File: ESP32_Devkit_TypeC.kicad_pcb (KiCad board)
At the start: 2 copper layers, 25.3 x 48.2 mm, 48 parts, among them J1 USB_C_Receptacle_USB2.0, J2 Conn_01x19, J3 Conn_01x19, Q1 SS8050, Q2 SS8050, SW1 EN, SW2 BOOT, U1 MP2359, U2 CH340G, U3 ESP32-PICO-D4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

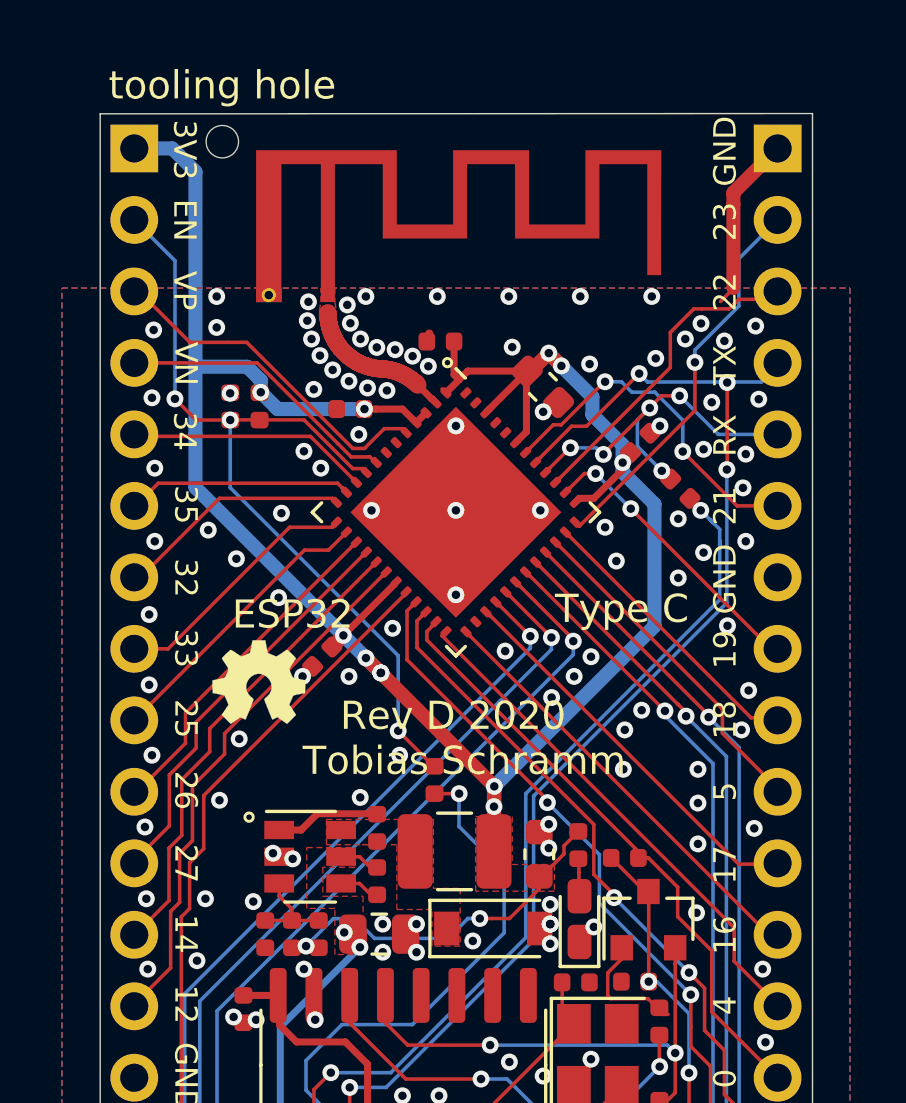
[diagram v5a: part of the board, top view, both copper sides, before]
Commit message: Rev E better bypassing
This revision improves upon the bypassing of the ESP32 Pico D4.
The previous bypassing was not satisfactory to me and I fear it
might cause issues under high load conditions.
Bypassing is improved by adding an additional 10uF capacitor to
each power pin.
Additionally a third 22uF capacitor has been added to icrease bulk
capacitance
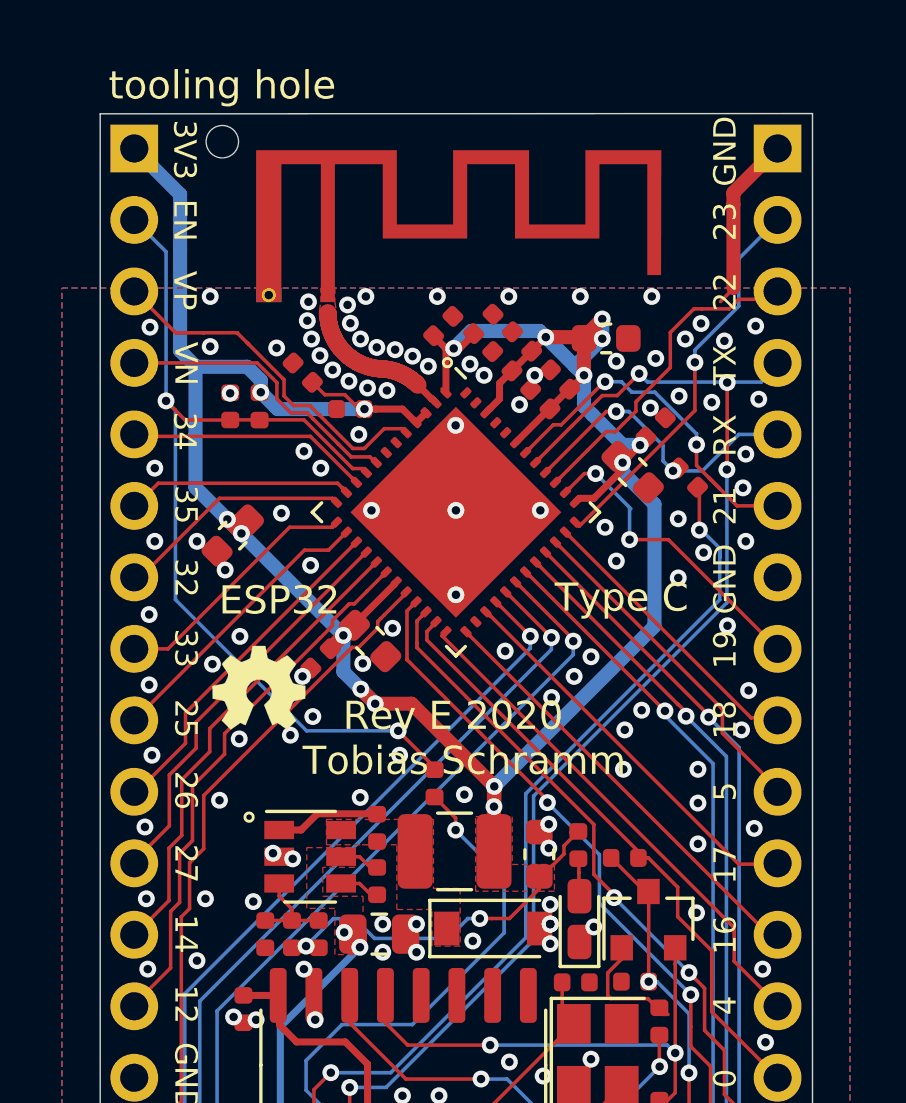
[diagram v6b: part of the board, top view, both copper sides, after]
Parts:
- added C17: 100 nF, Capacitor_SMD:C_0402_1005Metric, F.Cu at (101.7, 84.7)
- added C18: 100 nF, Capacitor_SMD:C_0402_1005Metric, F.Cu at (103.0, 86.0)
- added C19: 10uF, Capacitor_SMD:C_0402_1005Metric, F.Cu at (102.3, 84.0)
- added C20: 10uF, Capacitor_SMD:C_0402_1005Metric, F.Cu at (101.0, 83.4)
- added C21: 10uF, Capacitor_SMD:C_0402_1005Metric, F.Cu at (103.7, 85.3)
- added C22: 10uF, Capacitor_SMD:C_0402_1005Metric, F.Cu at (94.6, 85.1)
- added C23: 10uF, Capacitor_SMD:C_0603_1608Metric, F.Cu at (97.0, 94.6)
- added C24: 22 uF, Capacitor_SMD:C_0603_1608Metric, F.Cu at (92.1, 90.9)
- added C25: 10uF, Capacitor_SMD:C_0603_1608Metric, F.Cu at (106.3, 88.6)
- moved C13 2.83 mm to (105.3, 83.9), turned to 0 degrees
- moved C6 0.77 mm to (107.1, 87.1)
- moved C15 0.56 mm to (99.5, 83.5), turned to 225 degrees
- moved R4 0.48 mm to (108.2, 88.8)
- moved I2 0.20 mm to (93.0, 96.3)
- moved R11 0.12 mm to (99.2, 99.7)
- moved C16 0.08 mm to (95.2, 95.3)
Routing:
- net +3V3: track 95.0 -> 109.5 mm, vias 13 -> 18
- net /EN: track 30.2 -> 34.0 mm, vias 3 -> 2
- net /RXD: track 13.3 -> 11.1 mm, vias 5 -> 2
- net /IO19: track 10.5 -> 11.3 mm
- net Net-(C10-Pad2): track 48.7 -> 48.1 mm
- net /IO21: track 12.7 -> 13.2 mm
- net /VP: track 12.2 -> 12.8 mm
- net GND: track 6.74 -> 6.70 mm, vias 139 -> 145
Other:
- board text added: "Rev E 2020"
- board text removed: "Rev D 2020"

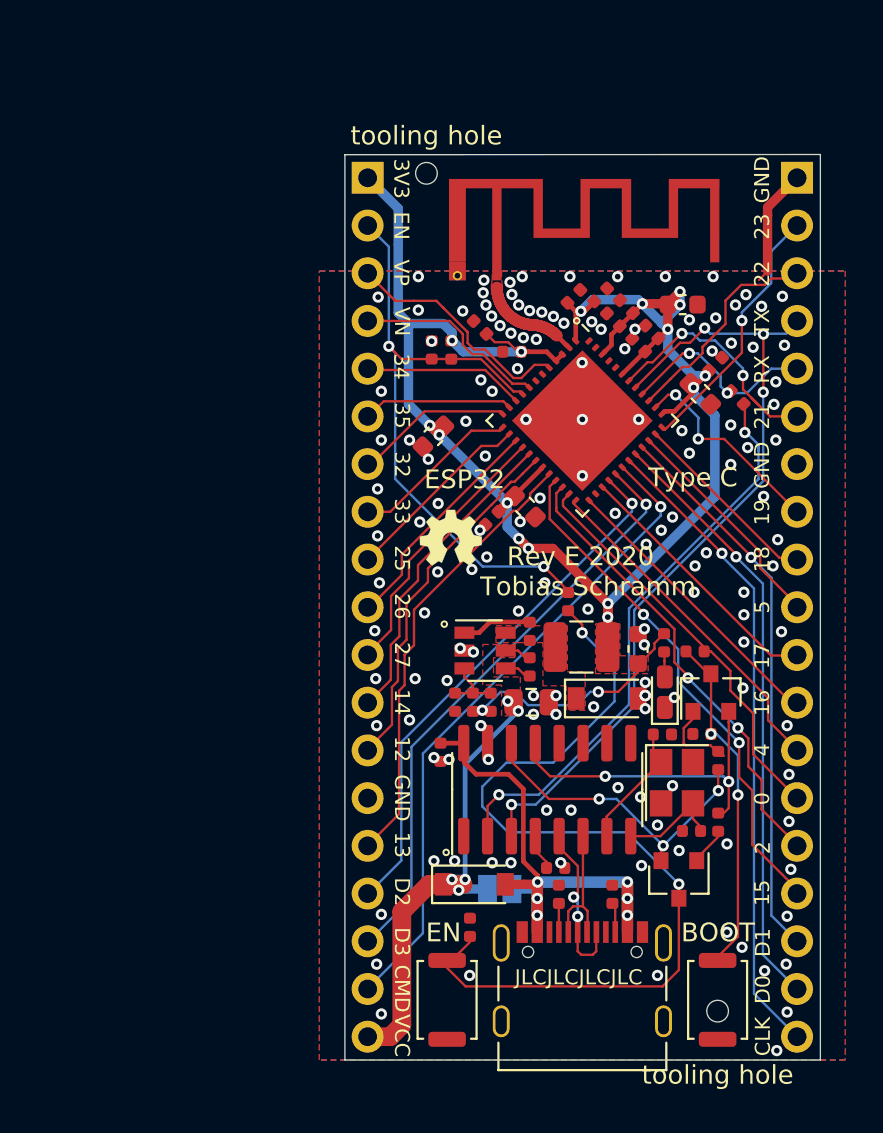
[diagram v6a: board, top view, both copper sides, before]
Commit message: Start revision F layout
The previous five revisions are not satisfactory. They have a number of
issues:

- Poor RF performance due to improper antenna placement and matching
- GPIO16 and GPIO17 are unusable, inherent problem with Pico D4
- Instability. Might be related to excessive power consumption due to
  improper antenna matching
- Changes in availability of LCSC parts

Overall those problems have prompted me to design a revision F of this
board. Most notably the ESP32 Pico D4 will be swapped for an ESP32-D0WD.
This will ensure the board actually behaves like a ESP32 DevKitC and
make it a true drop-in replacement. To ensure power and signal integrity
the new board will be a four layer one. Overall the board outline will
change slightly to allocate a suitable location for the antenna. With that
the height of the board will be closer to that of a DevKitC V1. Judging
from online listings the DevKitC V1 pinout still seems to be the most
popular one. Thus I will stick to that.
Also availability of cheap ESP32 development boards with USB Type C still
seems to be just as bad as back in 2020 when I designed the initial
revision of this board. Thus I think this new revision is a worthwhile
project.
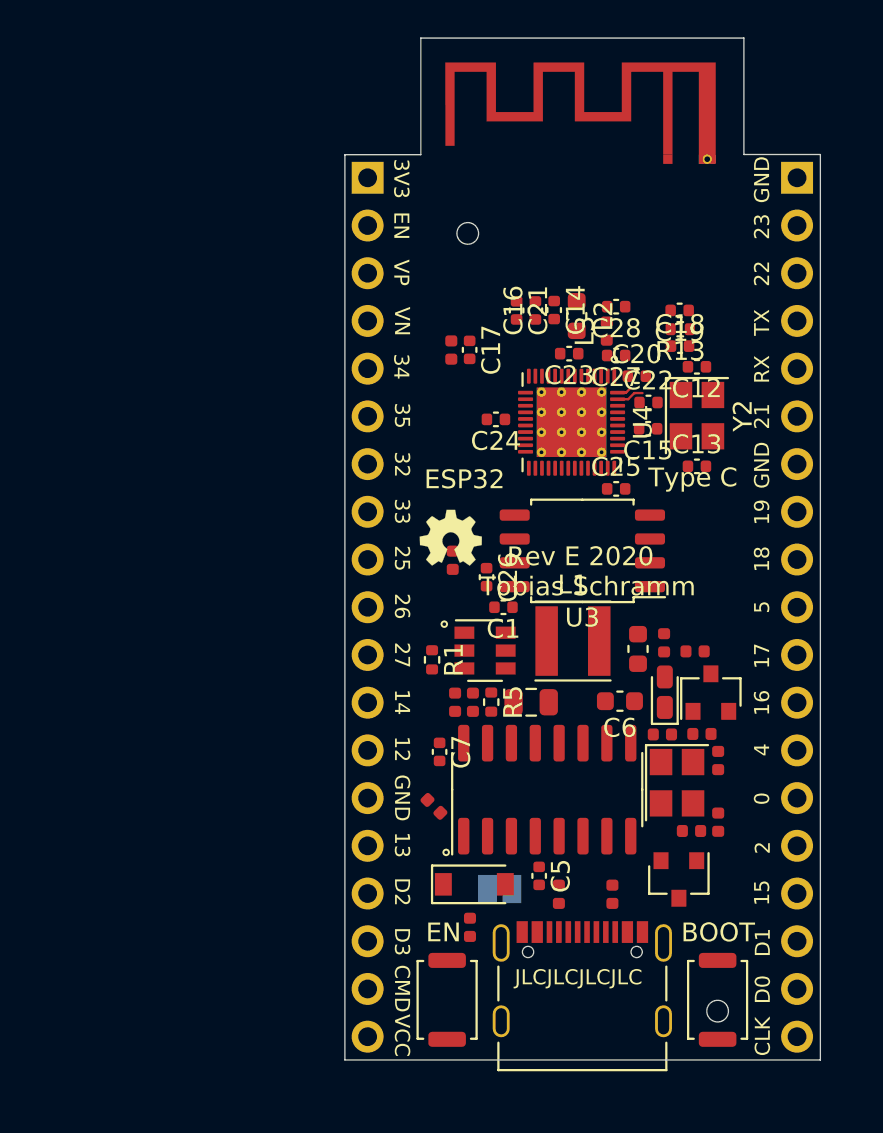
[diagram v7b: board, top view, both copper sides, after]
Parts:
- removed D2: B5819W, Diode_SMD:D_SOD-123
- added C26: 1uF, Capacitor_SMD:C_0402_1005Metric, F.Cu at (94.9, 98.4)
- added C27: DNP, Capacitor_SMD:C_0402_1005Metric, F.Cu at (101.8, 86.6)
- added C28: DNP, Capacitor_SMD:C_0402_1005Metric, F.Cu at (101.8, 84.0)
- added L2: 4.7nH, Inductor_SMD:L_0603_1608Metric, F.Cu at (99.7, 84.5)
- added L3: 0R, Inductor_SMD:L_0402_1005Metric, F.Cu at (101.3, 85.3)
- added R13: 20k, Resistor_SMD:R_0402_1005Metric, F.Cu at (105.2, 85.2)
- added U4: ESP32-D0WD, Package_DFN_QFN:QFN-48-1EP_5x5mm_P0.35mm_EP3.7x3.7mm_ThermalVias, F.Cu at (99.4, 90.2)
- added Y2: 40MHz, Crystal:Crystal_SMD_3225-4Pin_3.2x2.5mm, F.Cu at (106.1, 89.8)
- AE1: footprint Antenna_IFA:Antenna_IFA_2.4GHz_meandered -> Antenna_IFA:Antenna_IFA_2.4GHz_meandered_mirrored
- C1: value 10 nF -> 22nF
- C12: value 1uF -> 30pF
- C13: value 22 uF -> 30pF; footprint Capacitor_SMD:C_0603_1608Metric -> Capacitor_SMD:C_0402_1005Metric
- C14: value 100 nF -> 10uF
- C15, C16, C17: value 100 nF -> 1uF
- C18: value 100 nF -> 3.3nF
- C19: value 10uF -> 10nF
- C2, C4: value 22 pF -> 22pF
- C20, C21: value 10uF -> 100nF
- C22: value 10uF -> 100pF
- C23: value 10uF -> DNP; footprint Capacitor_SMD:C_0603_1608Metric -> Capacitor_SMD:C_0402_1005Metric
- C24: value 22 uF -> 100nF; footprint Capacitor_SMD:C_0603_1608Metric -> Capacitor_SMD:C_0402_1005Metric
- C25: value 10uF -> 100nF; footprint Capacitor_SMD:C_0603_1608Metric -> Capacitor_SMD:C_0402_1005Metric
- C3: value 10 uF -> 22uF 25V
- C5: value 100 nF -> 10nF
- C6: value 100 nF -> 22uF; footprint Capacitor_SMD:C_0402_1005Metric -> Capacitor_SMD:C_0603_1608Metric
- C7: value 100 nF -> 100nF
- C8: value 22 uF -> 22uF
- L1: value 4.7 uH -> 10uH; footprint Inductor_SMD:L_1210_3225Metric -> Inductor_SMD:L_Taiyo-Yuden_MD-4040
- R1, R10: value 100 kR -> 100k
- R11, R12, R4: value 330 R -> 330R
- R2, R3: value 5.1 kR -> 5.1k
- R5: value 49.9kR -> 100k
- R6: value 15 kR -> 22k
- R7, R8, R9: value 5.1kR -> 5.1k
- U3: value ESP32-PICO-D4 -> W25Q128JVS; footprint Package_ESP32:ESP32-Pico-D4 -> Package_SO:SOIC-8_5.23x5.23mm_P1.27mm
- moved R4 27.1 mm to (92.1, 110.6)
- moved C6 18.7 mm to (102.0, 105.0), turned to 180 degrees
- moved C12 14.1 mm to (106.1, 87.2), turned to 180 degrees
- moved C16 11.3 mm to (97.5, 84.2), turned to 90 degrees
- moved C22 9.81 mm to (103.5, 89.1), turned to 0 degrees
- moved C13 8.64 mm to (106.1, 92.5)
- moved C23 8.47 mm to (99.3, 86.5), turned to 180 degrees
- moved C15 8.08 mm to (103.5, 90.5), turned to 180 degrees
- moved C17 7.82 mm to (94.0, 86.3), turned to 270 degrees
- moved C21 7.29 mm to (96.5, 84.2), turned to 270 degrees
- moved U3 6.93 mm to (100.0, 97.0), turned to 180 degrees
- moved C25 6.76 mm to (101.8, 93.7), turned to 0 degrees
- moved R11 6.52 mm to (93.1, 97.5)
- moved AE1 6.20 mm to (92.4, 75.9)
- moved R1 5.21 mm to (92.0, 102.8)
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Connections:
- C12 pad 1: /EN -> GND
- C12 pad 2: GND -> Net-(C12-Pad2)
- C13 pad 1: +3V3 -> GND
- C13 pad 2: GND -> Net-(C13-Pad2)
- C14 pad 1: GND -> +3V3
- C14 pad 2: +3V3 -> GND
- C16 pad 1: +3V3 -> GND
- C16 pad 2: GND -> +3V3
- C17 pad 1: +3V3 -> GND
- C17 pad 2: GND -> /EN
- C18 pad 1: +3V3 -> Net-(C18-Pad1)
- C18 pad 2: GND -> Net-(C18-Pad2)
- C19 pad 1: +3V3 -> GND
- C19 pad 2: GND -> Net-(C18-Pad1)
- C20 pad 1: GND -> +3V3
- C20 pad 2: +3V3 -> GND
- C21 pad 1: GND -> +3V3
- C21 pad 2: +3V3 -> GND
- C23 pad 1: GND -> Net-(C23-Pad1)
- C23 pad 2: +3V3 -> GND
- C5 pad 1: Net-(C5-Pad1) -> +3V3
- C6 pad 1: GND -> +3V3
- C6 pad 2: +3V3 -> GND
- C7 pad 1: GND -> +3V3
- C7 pad 2: VBUS -> GND
- R1 pad 1: VCC -> Net-(R1-Pad1)
- R1 pad 2: Net-(R1-Pad2) -> VCC
- R5 pad 1: +3V3 -> Net-(C9-Pad2)
- R5 pad 2: Net-(C9-Pad2) -> +3V3
- U1 pad 4: Net-(R1-Pad2) -> Net-(R1-Pad1)
- U2 pad 16: VBUS -> +3V3
- U2 pad 4: Net-(C5-Pad1) -> +3V3
- U3 pad 1: +3V3 -> /CMD
- U3 pad 2: Net-(AE1-Pad1) -> /SD1
- U3 pad 3: +3V3 -> /SD2
- U3 pad 4: +3V3 -> GND
- U3 pad 5: /VP -> /SD0
- U3 pad 6: Net-(U3-Pad6) -> /CLK
- U3 pad 7: Net-(U3-Pad7) -> /SD3
- U3 pad 8: /VN -> /VDD_SDIO
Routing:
- net +3V3: track 109.5 -> 0.00 mm, vias 18 -> 0
- net Net-(C10-Pad2): track 48.1 -> 0.00 mm, vias 2 -> 0
- net /TXD: track 43.4 -> 0.00 mm, vias 4 -> 0
- net /CMD: track 35.1 -> 0.00 mm, vias 1 -> 0
- net /CLK: track 34.4 -> 0.00 mm, vias 1 -> 0
- net /EN: track 34.0 -> 0.00 mm, vias 2 -> 0
- net /SD0: track 32.2 -> 0.00 mm, vias 1 -> 0
- net /SD3: track 31.6 -> 0.00 mm, vias 1 -> 0
- net Net-(R4-Pad2): track 30.9 -> 0.00 mm, vias 2 -> 0
- net /SD1: track 29.7 -> 0.00 mm, vias 1 -> 0
- net /SD2: track 28.4 -> 0.00 mm, vias 1 -> 0
- net VCC: track 28.2 -> 0.00 mm, vias 5 -> 0
- net VBUS: track 28.2 -> 0.00 mm, vias 6 -> 0
- net /IO15: track 27.2 -> 0.00 mm, vias 2 -> 0
- net /IO2: track 24.9 -> 0.00 mm, vias 2 -> 0
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- removed copper zone on F.Cu, net +3V3
- removed copper zone on B.Cu, net GND
- removed copper zone on F.Cu, net GND
- removed copper zone on F.Cu, net Net-(AE1-Pad1)
- removed copper zone on F.Cu, net Net-(C1-Pad1)
- removed copper zone on F.Cu, net VCC
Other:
- board size 25.3 x 48.2 mm -> 25.3 x 54.4 mm
- copper layers 2 -> 4
- rule via_min_drill: 0.3 -> 0.2
- rule via_min_size: 0.6 -> 0.45

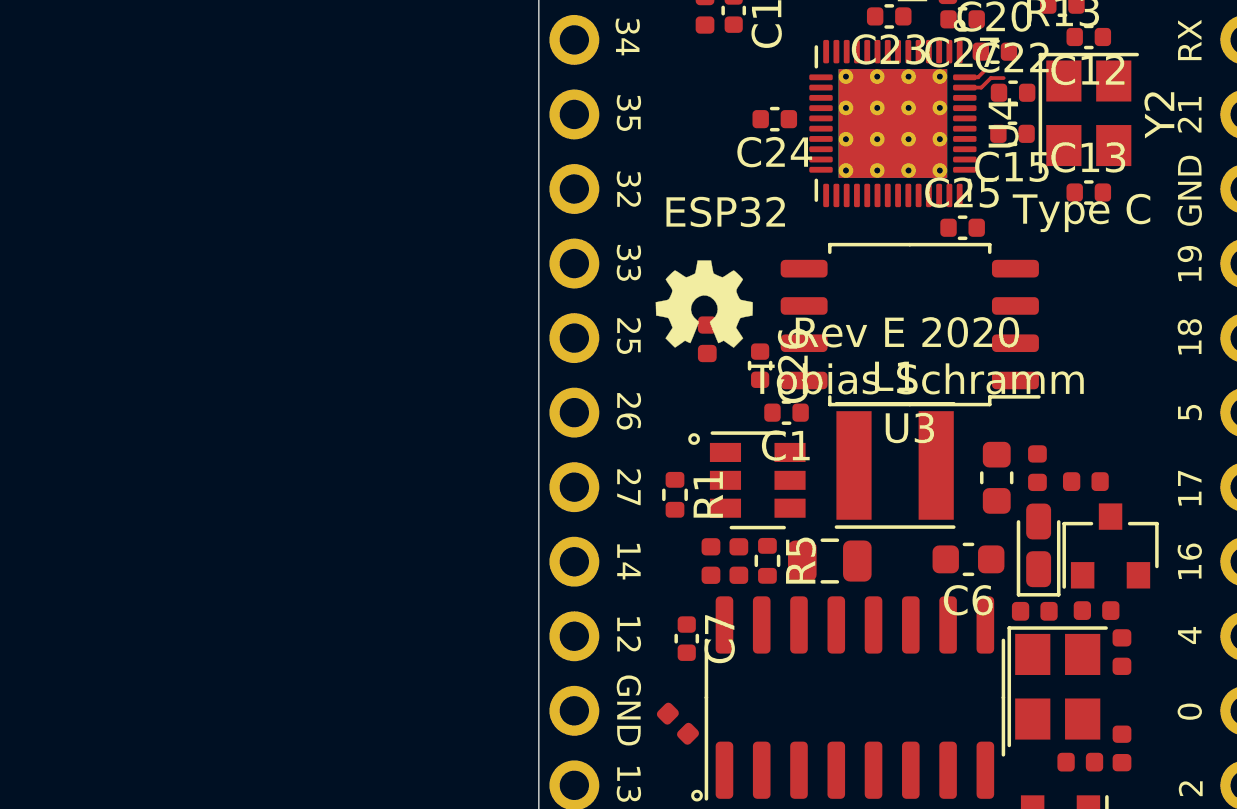
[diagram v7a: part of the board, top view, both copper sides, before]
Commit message: Layout primary step-down converter
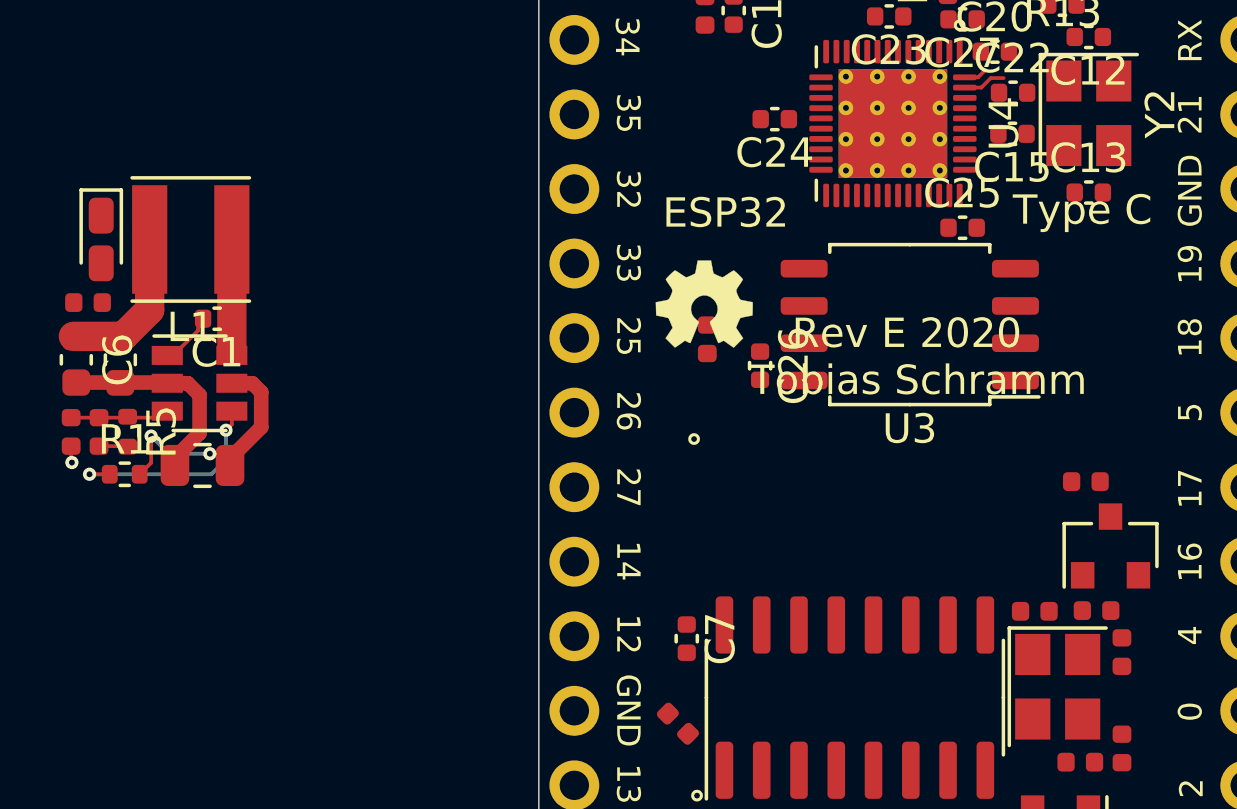
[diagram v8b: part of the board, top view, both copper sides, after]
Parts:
- U1: value MP2359 -> SD8942
- moved D3 33.6 mm to (72.5, 94.1), turned to 270 degrees
- moved R9 32.8 mm to (72.0, 96.2), turned to 0 degrees
- moved C6 31.2 mm to (71.6, 98.2), turned to 270 degrees
- moved C8 30.1 mm to (73.1, 98.2), turned to 270 degrees
- moved L1 25.2 mm to (75.5, 94.1), turned to 180 degrees
- moved R5 22.2 mm to (73.3, 100.7)
- moved C9 22.2 mm to (72.4, 100.7)
- moved R6 22.2 mm to (71.4, 100.7)
- moved C3 21.6 mm to (75.9, 101.8), turned to 0 degrees
- moved C1 19.7 mm to (76.4, 96.8)
- moved U1 19.3 mm to (75.8, 99.0)
- moved R1 18.8 mm to (73.2, 102.1), turned to 0 degrees
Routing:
- net VCC: track 0.00 -> 8.74 mm, vias 0 -> 2
- net GND: track 0.00 -> 7.77 mm, vias 0 -> 1
- net Net-(R1-Pad1): track 0.00 -> 7.28 mm, vias 0 -> 2
- net +3V3: track 0.00 -> 6.34 mm
- net Net-(C1-Pad1): track 0.00 -> 3.75 mm
- net Net-(C9-Pad2): track 0.00 -> 3.38 mm
- net Net-(C1-Pad2): track 0.00 -> 1.90 mm
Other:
- net class Default: via_dia 0.6 -> 0.45; via_drill 0.3 -> 0.2
